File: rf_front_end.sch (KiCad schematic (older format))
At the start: 64 parts, among them Q1 MOSFET_P, U14 MAX5864, U15 MAX2830

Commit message: retoque casi finales
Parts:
- removed FB2: FILTER, symbol hackrf-one-packages:FILTER
- added C111: 33pF, Capacitor_SMD:C_0603_1608Metric_Pad1.05x0.95mm_HandSolder, symbol Device:C
- added C112: 47pF, Capacitor_SMD:C_0603_1608Metric_Pad1.05x0.95mm_HandSolder, symbol Device:C
- added C113, C114, C115, C116, C117, C122: 100nF, Capacitor_SMD:C_0603_1608Metric_Pad1.05x0.95mm_HandSolder, symbol Device:C
- added C118, C119: 0, Capacitor_SMD:C_0603_1608Metric_Pad1.05x0.95mm_HandSolder, symbol BAT2032:C
- added C120: 100pF, Capacitor_SMD:C_0603_1608Metric_Pad1.05x0.95mm_HandSolder, symbol Device:C
- added C121: 2.2nF, Capacitor_SMD:C_0603_1608Metric_Pad1.05x0.95mm_HandSolder, symbol Device:C
- added C123: 68pF, Capacitor_SMD:C_0603_1608Metric_Pad1.05x0.95mm_HandSolder, symbol Device:C
- added J7, J8: Conn_Coaxial, library:TAOGLAS_EMPCB.SMAFSTJ.B.HT, symbol Connector:Conn_Coaxial
- added R18: 1k, Resistor_SMD:R_0603_1608Metric_Pad1.05x0.95mm_HandSolder, symbol BAT2032:R
- added R19: 1.2k, Resistor_SMD:R_0603_1608Metric_Pad1.05x0.95mm_HandSolder, symbol BAT2032:R
- added R20: 750, Resistor_SMD:R_0603_1608Metric_Pad1.05x0.95mm_HandSolder, symbol BAT2032:R
- added T1, T2: BALUN, library:HHM1711E1, symbol power-rescue:BALUN-hackrf-one-rescue
- C100, C101, C102, C103, C104, C105, C106, C107, C75, C76, C77, C78, C79, C80, C81, C82, C83, C84, C86, C87, C90, C91, C92, C93, C94, C95, C96, C97, C98, C99: footprint (none) -> Capacitor_SMD:C_0603_1608Metric_Pad1.05x0.95mm_HandSolder
- C108, C109: renamed from C?; digikey (none) -> 1276-2218-1-ND
- D11: footprint (none) -> LED_SMD:LED_0603_1608Metric_Pad1.05x0.95mm_HandSolder
- FB1: footprint (none) -> Inductor_SMD:L_0805_2012Metric_Pad1.15x1.40mm_HandSolder; symbol hackrf-one-packages:FILTER -> power-rescue:FILTER-hackrf-one-packages; digikey (none) -> BLM21PG221SN1D
- Q1: footprint (none) -> library:SOT103P240X110-3N; symbol hackrf-one-packages:MOSFET_P -> power-rescue:MOSFET_P-hackrf-one-packages; digikey (none) -> DMP2305UDICT-ND
- R42, R43, R52, R53, R55: footprint (none) -> Resistor_SMD:R_0603_1608Metric_Pad1.05x0.95mm_HandSolder
- R54: footprint Resistor_SMD:R_0402_1005Metric -> Resistor_SMD:R_0603_1608Metric_Pad1.05x0.95mm_HandSolder
- R59, R61: renamed from R?; footprint Resistor_SMD:R_0402_1005Metric -> Resistor_SMD:R_0603_1608Metric_Pad1.05x0.95mm_HandSolder; DIGIKEY RMSF0402JT39R0CT-ND -> 311-39.0HRCT-ND
- U14: footprint (none) -> library:MAX5864ETM&plus_; symbol hackrf-one-rescue:MAX5864 -> power-rescue:MAX5864-hackrf-one-rescue
- U15: footprint (none) -> library:MAX2830ETM&plus_; symbol quacho-packages:MAX2830 -> power-rescue:MAX2830-quacho-packages
- U16: renamed from U?; symbol hackrf-one-rescue:SI5351C -> power-rescue:SI5351C-hackrf-one-rescue; digikey (none) -> 336-5160-1-ND
- gave numbers to parts that had none: 6
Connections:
- net labels added: CS_AD, GPIO_INTR, I2C_00, I2C_01, I2C_0[0..1], I2C_SCL, I2C_SDA, SPI1[1..6], SPI1_CS_AD, SPI1_CS_RF, SPI1_MISO, SPI1_MOSI, SPI1_RSSI, SPI1_SCK, XTAL, rf_!SHDN, rf_ANTSEL, rf_LD, rf_RSSI, rf_RXHP, rf_RXTX, rf_TUNE, vcc_STM32
- net labels removed: adCLK, adCS, adCSK, adMOSI
- wire segments 264 -> 349
- no-connect marks 5 -> 15
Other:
- moved on the sheet: C100, C101, C102, C103, C104, C105, C106, C107, C75, C76, C77, C78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

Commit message: diseño de esquematico
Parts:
- removed C100, C99: 22pf, Capacitor_SMD:C_0603_1608Metric_Pad1.05x0.95mm_HandSolder, symbol BAT2032:C
- removed C107, C87, C91, C93: 100nF, Capacitor_SMD:C_0603_1608Metric_Pad1.05x0.95mm_HandSolder, symbol Device:C
- removed C110: C, Capacitor_SMD:C_0603_1608Metric_Pad1.05x0.95mm_HandSolder, symbol BAT2032:C
- removed C86, C90, C92: 2.2uF, Capacitor_SMD:C_0603_1608Metric_Pad1.05x0.95mm_HandSolder, symbol Device:C
- C88: renamed from C85; value 330nf -> 330nF
- C93: renamed from C88; value 330nf -> 330nF
- C94: renamed from C89; value 330nf -> 330nF
- R33: renamed from R60; footprint Resistor_SMD:R_0402_1005Metric -> Resistor_SMD:R_0603_1608Metric_Pad1.05x0.95mm_HandSolder
- U14: renamed from U16; footprint (none) -> library:QFN50P300X300X60-21N
- Y3: footprint library:GSG-XTAL3.2x2.5m -> library:GSG-XTAL3.2x2.5mm
- renumbered C116 to C100, C117 to C101, C94 to C102, C95 to C103, C96 to C104, C97 to C105, C98 to C106, C101 to C107, C102 to C108, C118 to C109, C119 to C110, C103 to C111, C104 to C112, C105 to C113, C106 to C116, C120 to C118, C121 to C119, C122 to C120, C123 to C121, C75 to C73, C78 to C74, C108 to C75, C77 to C76, C76 to C77, C109 to C78, C80 to C79, C79 to C80, C82 to C83, C83 to C84, C84 to C85, C111 to C86, C112 to C89, C113 to C92, C114 to C96, C115 to C98, D11 to D12, R56 to R27, R42 to R28, R57 to R29, R58 to R30, R43 to R31, R59 to R32, R61 to R34, R44 to R35, R45 to R36, R46 to R37, R47 to R38, R48 to R39, R49 to R40, R50 to R41, R51 to R42, R18 to R43, R52 to R44, R53 to R45, R19 to R46, R54 to R47, R55 to R48, R20 to R49, U14 to U15, U15 to U16
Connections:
- net labels removed: CS_AD, I2C_00, I2C_01, I2C_0[0..1], SPI1[1..6]
- wire segments 349 -> 316
- no-connect marks 15 -> 16
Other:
- moved on the sheet: C102, C103, C104, C105, C106, C107, C108, C111, C112, C113, C116, C75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

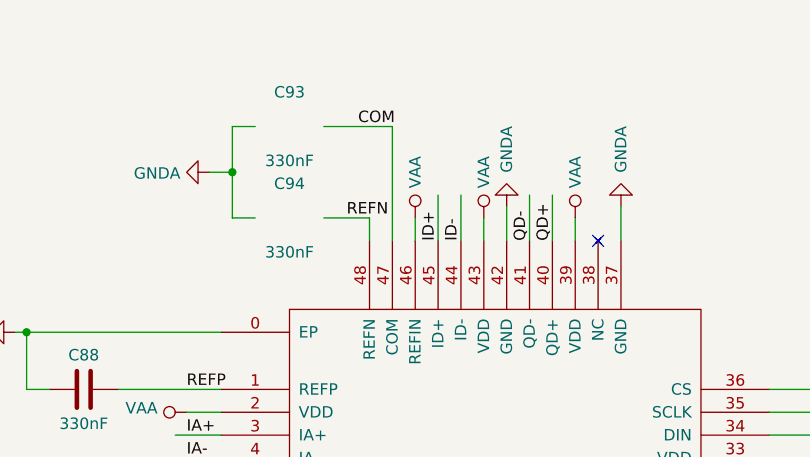
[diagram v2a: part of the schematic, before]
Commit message: diseño de esquematico fm
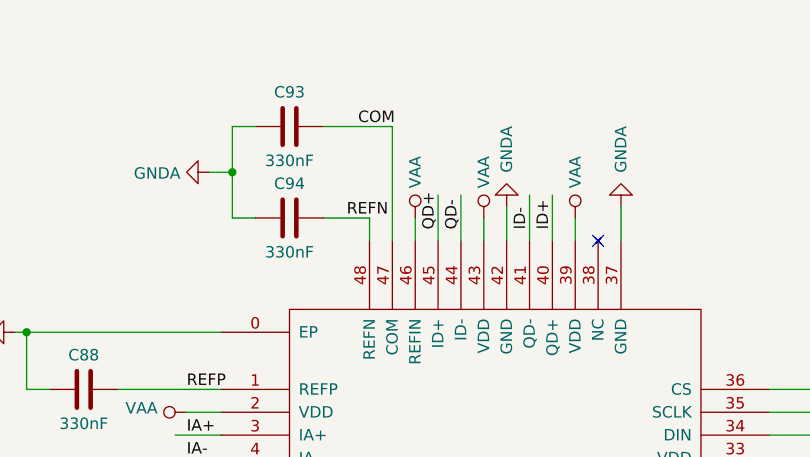
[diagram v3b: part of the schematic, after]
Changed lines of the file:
@@
 Wire Wire Line
 	4800 3600 4600 3600
-Text Label 5750 2050 1    50   ~ 0
+Text Label 6250 2000 1    50   ~ 0
 ID+
-Text Label 5850 2050 1    50   ~ 0
+Text Label 6150 2000 1    50   ~ 0
 ID-
-Text Label 6150 2050 1    50   ~ 0
+Text Label 5850 2000 1    50   ~ 0
 QD-
-Text Label 6250 2050 1    50   ~ 0
+Text Label 5750 2000 1    50   ~ 0
 QD+
 Text Label 4650 2900 0    50   ~ 0
@@
 $Comp
 L BAT2032:C C93
-U 1 0 5DBF0626
+U 1 1 5DBF0626
 P 5100 1550
 F 0 "C93" V 4950 1550 50  0000 C CNN
@@
 $Comp
 L BAT2032:C C94
-U 1 0 5DBE5B62
+U 1 1 5DBE5B62
 P 5100 1950
 F 0 "C94" V 4950 1950 50  0000 C CNN
@@
 Wire Wire Line
 	14650 3450 14750 3450
-$Comp
-L BAT2032:R R47
-U 1 1 5CFFD8F9
-P 14900 3450
-F 0 "R47" V 14850 3300 50  0000 C CNN
-F 1 "0" V 14900 3450 50  0000 C CNN
-F 2 "Resistor_SMD:R_0603_1608Metric_Pad1.05x0.95mm_HandSolder" V 14830 3450 50  0001 C CNN
-F 3 "~" H 14900 3450 50  0001 C CNN
-F 4 "RMCF0402ZT0R00CT-ND" V 14900 3450 50  0001 C CNN "digikey"
-	1    14900 3450
-	0    1    1    0
-$EndComp
 $Comp
 L BAT2032:R R44
@@
 Wire Wire Line
 	11250 2400 13200 2400
+$Comp
+L BAT2032:R R47
+U 1 1 5CFFD8F9
+P 14900 3450
+F 0 "R47" V 14850 3300 50  0000 C CNN
+F 1 "0" V 14900 3450 50  0000 C CNN
+F 2 "Resistor_SMD:R_0603_1608Metric_Pad1.05x0.95mm_HandSolder" V 14830 3450 50  0001 C CNN
+F 3 "~" H 14900 3450 50  0001 C CNN
+F 4 "RMCF0402ZT0R00CT-ND" V 14900 3450 50  0001 C CNN "digikey"
+	1    14900 3450
+	0    1    1    0
+$EndComp
 $EndSCHEMATC
